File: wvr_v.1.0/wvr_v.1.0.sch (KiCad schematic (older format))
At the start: 43 parts, among them J1 10118192-0001LF, J2 Conn_01x11, J3 Conn_01x11, SW1 SW_Push, U1 TCMT1101, U2 LM1117-3.3, U3 KLM8G1GETF, U4 PCM5102, U5 ESP32-WROVER-B_(16MB)

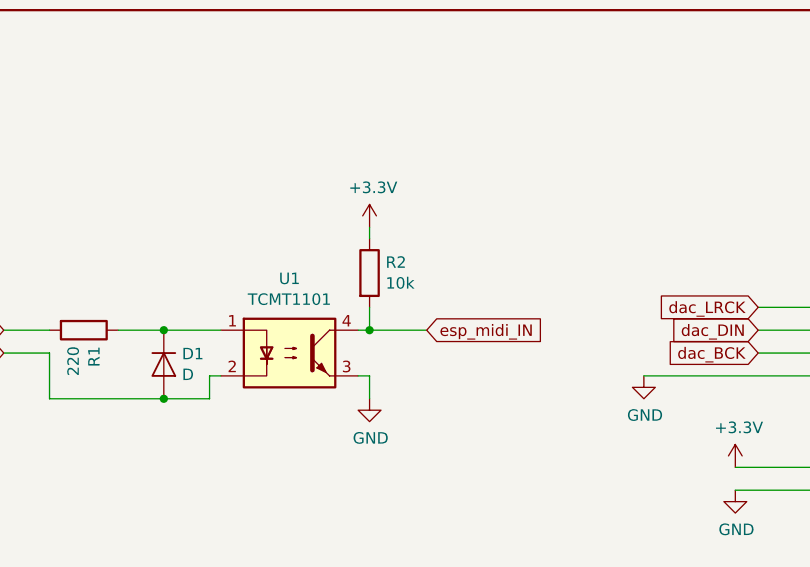
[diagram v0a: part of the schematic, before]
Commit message: update schematic resistor values
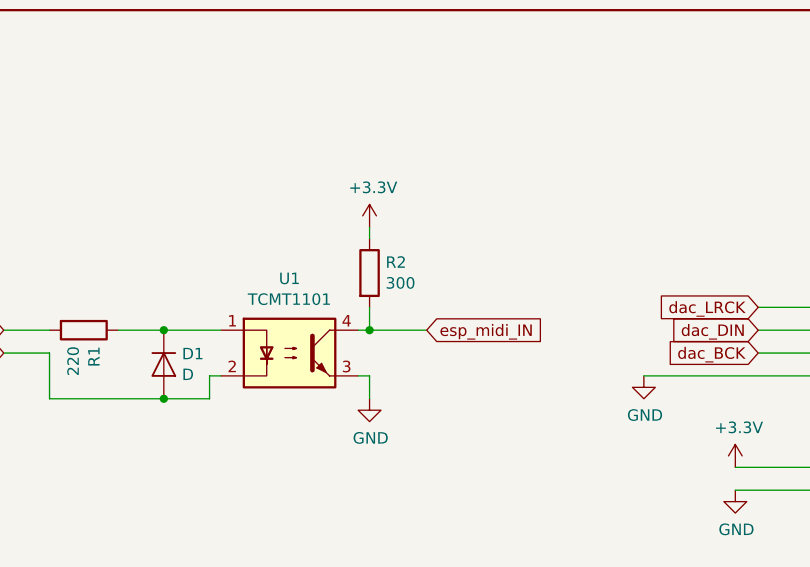
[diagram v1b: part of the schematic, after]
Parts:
- R2: value 10k -> 300
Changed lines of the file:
@@
 P 9050 6150
 F 0 "R2" H 9120 6196 50  0000 L CNN
-F 1 "10k" H 9120 6105 50  0000 L CNN
+F 1 "300" H 9120 6105 50  0000 L CNN
 F 2 "Resistor_SMD:R_0402_1005Metric" V 8980 6150 50  0001 C CNN
 F 3 "~" H 9050 6150 50  0001 C CNN

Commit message: update
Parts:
- added R14: 1K, Resistor_SMD:R_0603_1608Metric_Pad1.05x0.95mm_HandSolder, symbol Device:R
- added U6: SeeeduinoXIAO, Seeeduino XIAO KICAD:Seeeduino XIAO-MOUDLE14P-2.54-21X17.8MM, symbol Seeeduino_XIAO:SeeeduinoXIAO
- J1: footprint Waver:USB-MICRO-B_C40942 -> wvr_v.1.0:USB-MICRO-B_C40942
- U3: footprint Waver:KLM8G1GETF_ALL_PADS -> wvr_v.1.0:KLM8G1GETF_ALL_PADS
- U5: footprint Waver:XCVR_ESP32-WROVER-B_(16MB) -> wvr_v.1.0:XCVR_ESP32-WROVER-B_(16MB)
- renumbered R to R13
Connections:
- net +5V: now also U6.14 (5V)
- net GND: now also U6.13 (GND)
- net esp_GPIO21: now also R14.1
- new net: R14.2, U6.7 (PB08_A6_D6_TX)
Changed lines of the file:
@@
 F 0 "J1" H 4042 5835 50  0000 C CNN
 F 1 "10118192-0001LF" H 4042 5926 50  0000 C CNN
-F 2 "Waver:USB-MICRO-B_C40942" H 4100 6400 50  0001 L BNN
+F 2 "wvr_v.1.0:USB-MICRO-B_C40942" H 4100 6400 50  0001 L BNN
 F 3 "Manufacturer Recommendation" H 4100 6400 50  0001 L BNN
 F 4 "B" H 4100 6400 50  0001 L BNN "Field4"
@@
 	10650 10100 10450 10100
 $Comp
-L Device:R R
+L Device:R R13
 U 1 1 5EB54D9A
 P 9900 10100
-F 0 "R" V 9693 10100 50  0000 C CNN
+F 0 "R13" V 9693 10100 50  0000 C CNN
 F 1 "100R" V 9784 10100 50  0000 C CNN
 F 2 "Resistor_SMD:R_0402_1005Metric" V 9830 10100 50  0001 C CNN
@@
 F 0 "U5" H 8250 5167 50  0000 C CNN
 F 1 "ESP32-WROVER-B_(16MB)" H 8250 5076 50  0000 C CNN
-F 2 "Waver:XCVR_ESP32-WROVER-B_(16MB)" H 8250 3700 50  0001 L BNN
+F 2 "wvr_v.1.0:XCVR_ESP32-WROVER-B_(16MB)" H 8250 3700 50  0001 L BNN
 F 3 "1.1" H 8250 3700 50  0001 L BNN
 F 4 "C529591" H 8250 3700 50  0001 C CNN "LCSC"
@@
 F 0 "U3" H 8630 7715 50  0000 C CNN
 F 1 "KLM8G1GETF" H 8630 7624 50  0000 C CNN
-F 2 "Waver:KLM8G1GETF_ALL_PADS" H 8550 7600 50  0001 C CNN
+F 2 "wvr_v.1.0:KLM8G1GETF_ALL_PADS" H 8550 7600 50  0001 C CNN
 F 3 "" H 8550 7600 50  0001 C CNN
 F 4 "C499918" H 8550 7600 50  0001 C CNN "LCSC"
@@
 	12300 8900 11750 8900
 Connection ~ 11750 8900
+$Comp
+L Seeeduino_XIAO:SeeeduinoXIAO U6
+U 1 1 62402C4C
+P 2100 7400
+F 0 "U6" H 900 6400 50  0000 C CNN
+F 1 "SeeeduinoXIAO" H 950 6250 50  0000 C CNN
+F 2 "Seeeduino XIAO KICAD:Seeeduino XIAO-MOUDLE14P-2.54-21X17.8MM" H 1750 7600 50  0001 C CNN
+F 3 "" H 1750 7600 50  0001 C CNN
+	1    2100 7400
+	1    0    0    -1
+$EndComp
+$Comp
+L power:+5V #PWR0121
+U 1 1 624052E8
+P 3150 6900
+F 0 "#PWR0121" H 3150 6750 50  0001 C CNN
+F 1 "+5V" H 3165 7073 50  0000 C CNN
+F 2 "" H 3150 6900 50  0001 C CNN
+F 3 "" H 3150 6900 50  0001 C CNN
+	1    3150 6900
+	1    0    0    -1
+$EndComp
+$Comp
+L power:GND #PWR0122
+U 1 1 6242112F
+P 3150 7150
+F 0 "#PWR0122" H 3150 6900 50  0001 C CNN
+F 1 "GND" H 3155 6977 50  0000 C CNN
+F 2 "" H 3150 7150 50  0001 C CNN
+F 3 "" H 3150 7150 50  0001 C CNN
+	1    3150 7150
+	1    0    0    -1
+$EndComp
+Text GLabel 800  7800 1    50   Input ~ 0
+esp_GPIO21
+$Comp
+L Device:R R14
+U 1 1 624838FB
+P 950 7850
+F 0 "R14" V 743 7850 50  0000 C CNN
+F 1 "1K" V 834 7850 50  0000 C CNN
+F 2 "Resistor_SMD:R_0603_1608Metric_Pad1.05x0.95mm_HandSolder" V 880 7850 50  0001 C CNN
+F 3 "~" H 950 7850 50  0001 C CNN
+	1    950  7850
+	0    -1   -1   0
+$EndComp
+Wire Wire Line
+	800  7800 800  7850
+Wire Wire Line
+	1250 7850 1100 7850
+Wire Wire Line
+	3150 7150 3150 7100
+Wire Wire Line
+	3150 7100 2900 7100
+Wire Wire Line
+	3150 6900 3150 6950
+Wire Wire Line
+	3150 6950 2900 6950
 $EndSCHEMATC
